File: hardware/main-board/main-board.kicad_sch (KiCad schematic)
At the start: 79 parts, among them J1 Conn_01x04_Socket, J2 Conn_01x04_Socket, J3 Conn_01x04_Socket, J4 Conn_01x04_Socket, J5 USB_C_Receptacle_USB2.0_16P, J6 Conn_01x02_MountingPin, J7 Conn_01x07_Socket, Q1 DMG2305UX, SW1 SW_SPDT, SW3 SW_SPDT, SW5 SW_Push, SW66 SW_Push, SW7 SW_Push, SW8 SW_Push, U1 ESP32-C6-MINI-1/U, U2 USBLC6-2SC6, U3 AP2112K-3.3, U4 TP4056-42-ESOP8, U5 AP22815AWT-7

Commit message: Added overvoltage protection to schematic
Layout Needs to be rerouted
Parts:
- renumbered D14 to D12, D12 to D8, F2 to F1
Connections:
- net +5V: no longer U2.5 (VBUS)
- net VBUS_PROTECTION_IN: now also U2.5 (VBUS)
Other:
- note added: "USB-C VBUS Protection with 1.5A Fuse"
- note added: "USB-C with ESD protection on D+ and D-"
- note removed: "Rename new parts with old numbering to keep parts"
- note removed: "U2 ESD protection Should be after VBUS protection or befor ?"
- note removed: "USB-C VBUS Protection"
- note removed: "USB-C with ESD Protection and 1.5A Fuse"
- moved on the sheet: C13, C14, C16, C3, C6, C9, D5, D6, D7, D8, F1, H1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

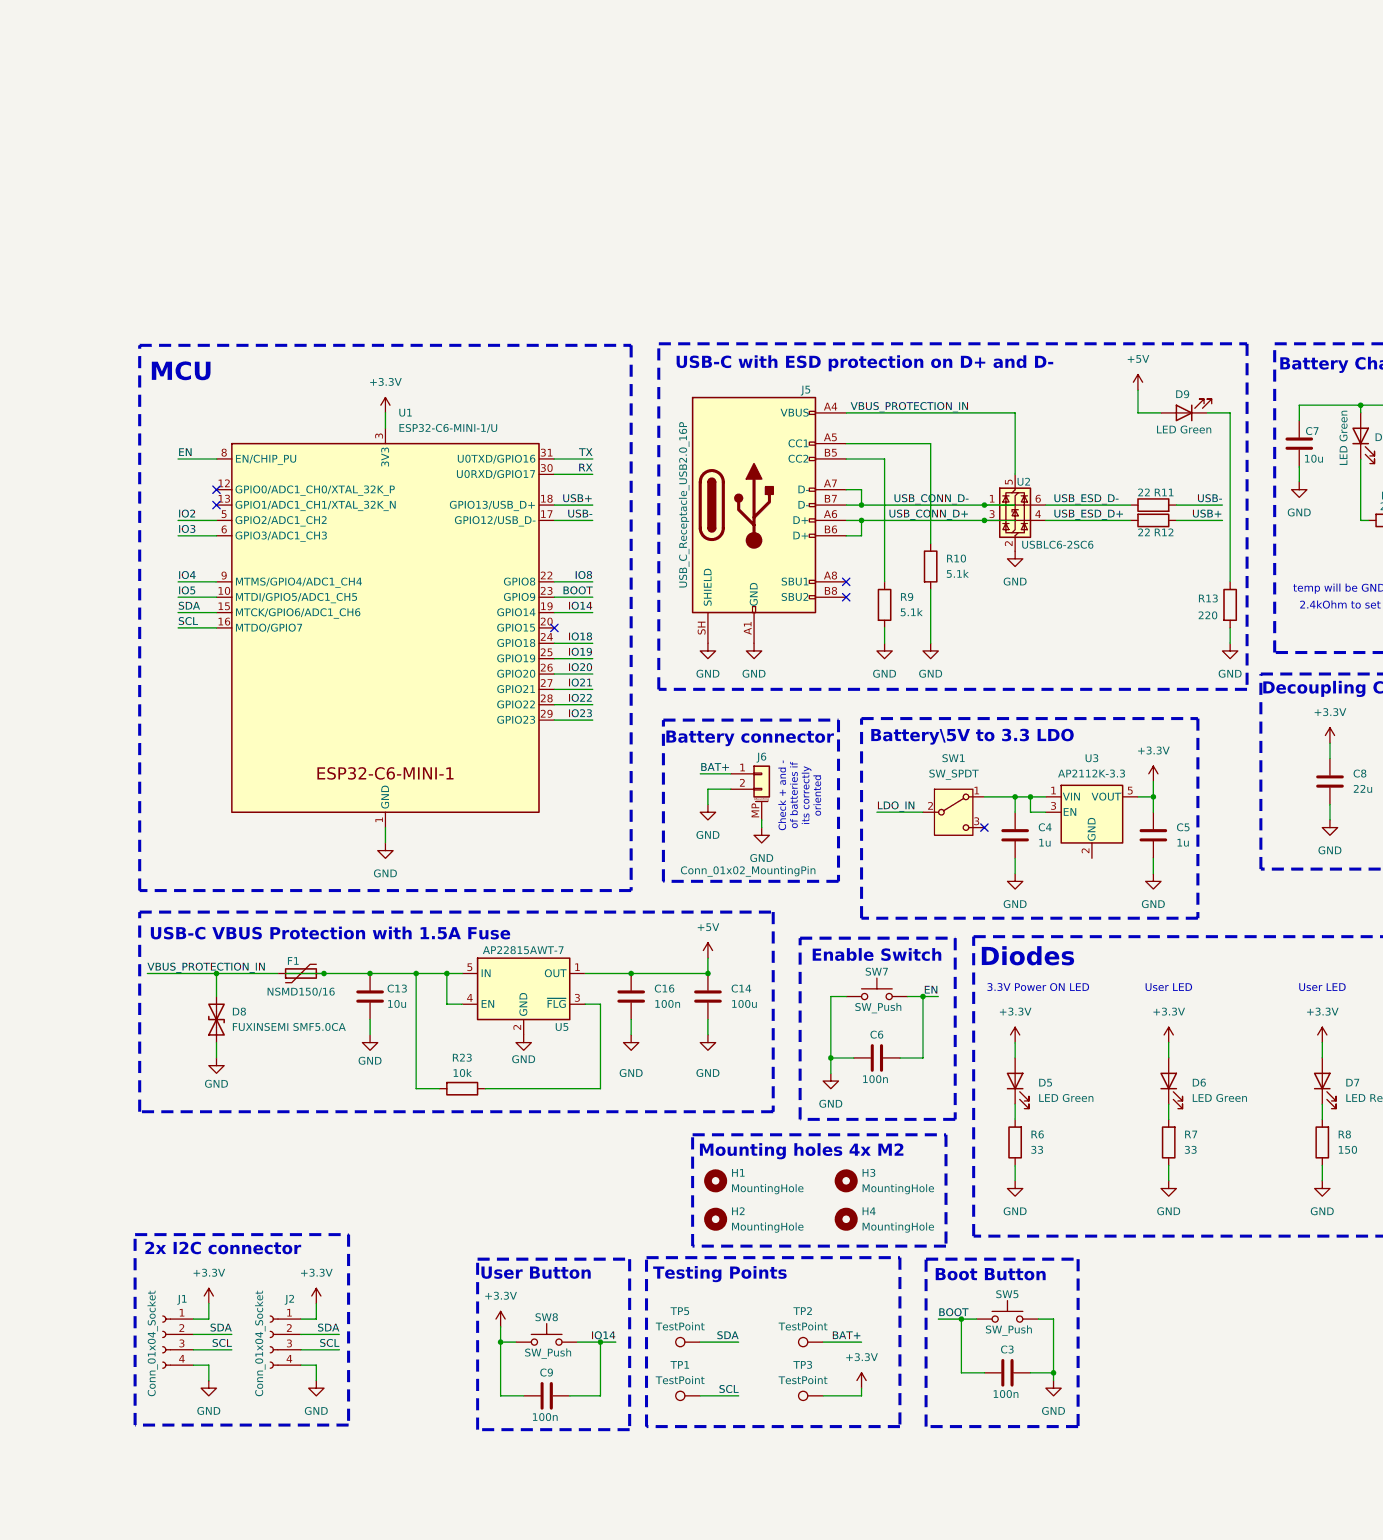
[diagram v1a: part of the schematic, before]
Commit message: After deciding we wont include OVP in this design, so i removed it from active schematic and check if everything is alright in pcb
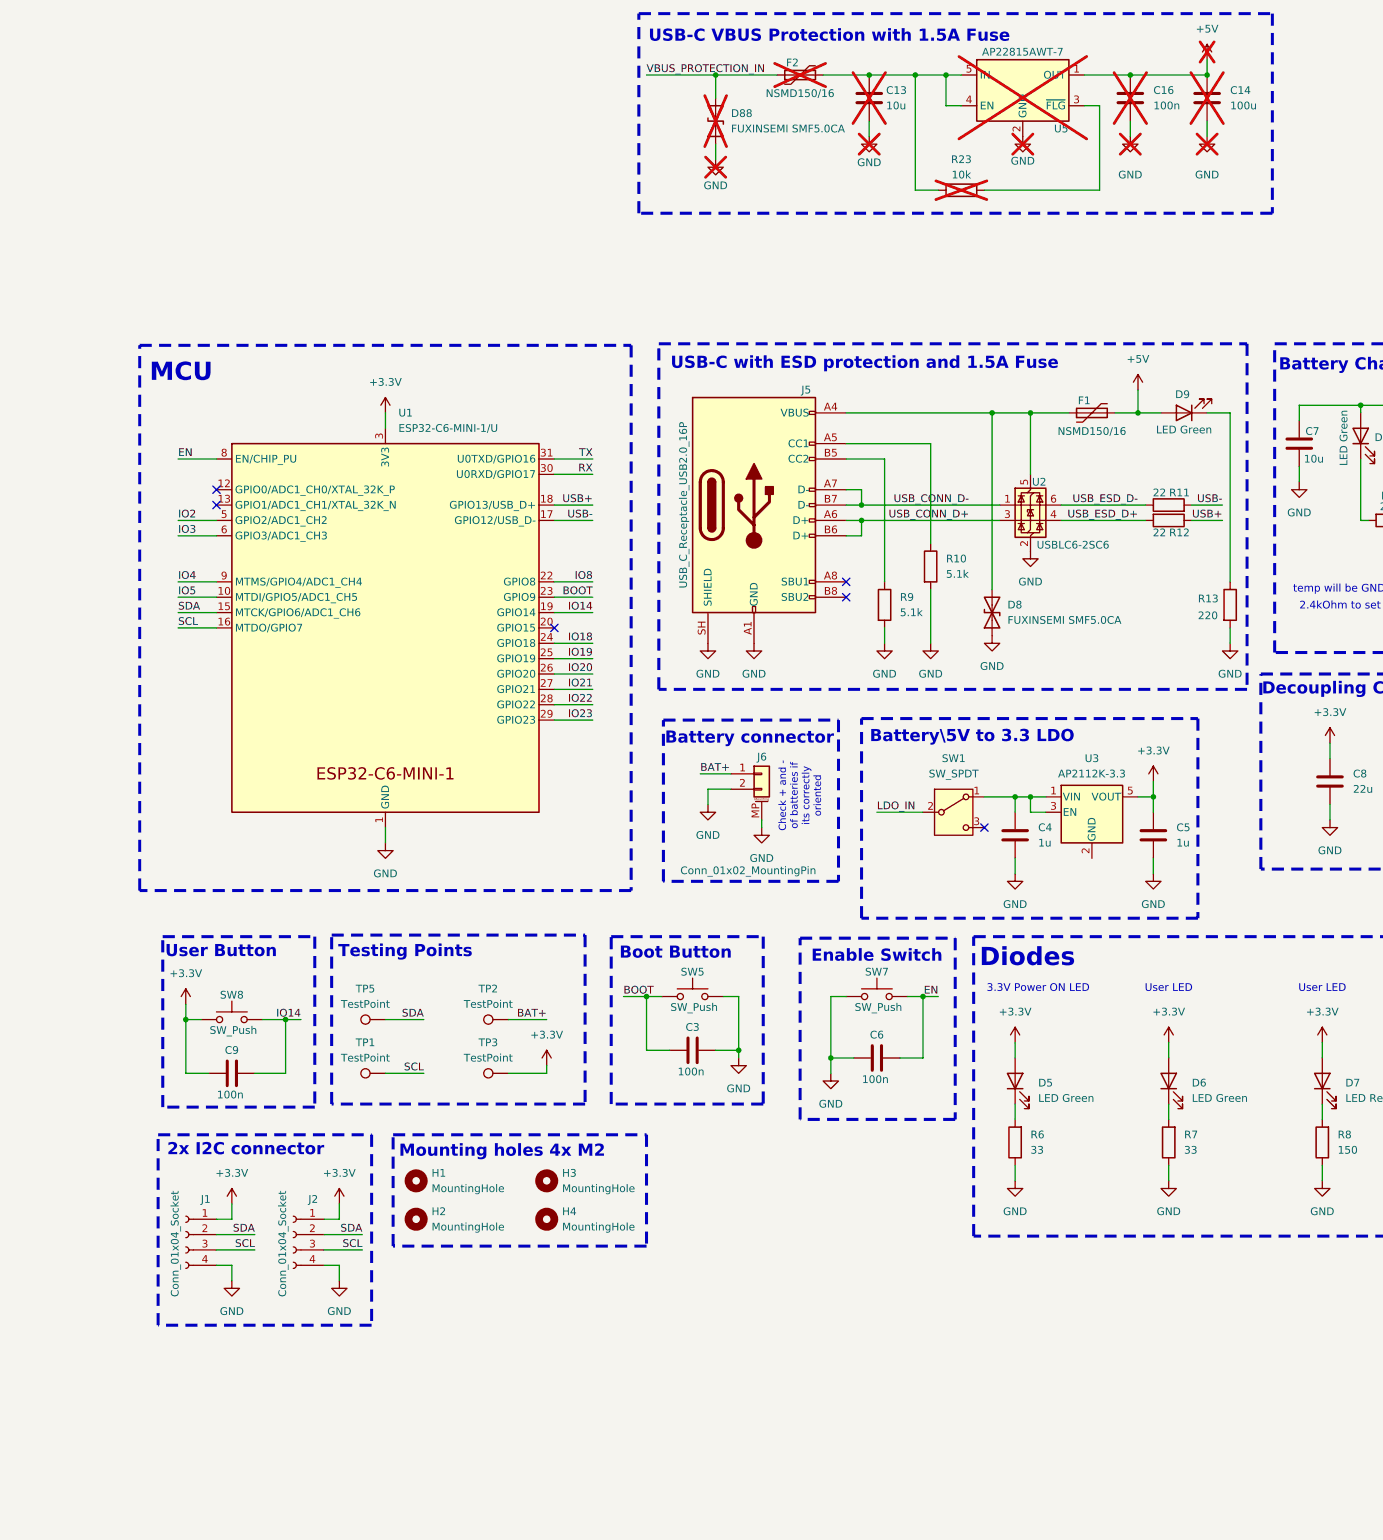
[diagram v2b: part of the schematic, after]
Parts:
- added D8: FUXINSEMI SMF5.0CA, Diode_SMD:D_SOD-123, symbol Device:D_TVS
- added F1: NSMD150/16, Fuse:Fuse_1206_3216Metric_Pad1.42x1.75mm_HandSolder, symbol Device:Polyfuse
- C13, C14, C16, R23, U5: now not fitted; now left out of the parts list
- D88: renamed from D8; now not fitted; now left out of the parts list
- F2: renamed from F1; now not fitted; now left out of the parts list
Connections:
- net +5V: now also F1.2
- net GND: now also D8.1 (A1)
- net VBUS_PROTECTION_IN: no longer J5.A4 (VBUS), J5.A9 (VBUS), J5.B4 (VBUS), J5.B9 (VBUS), U2.5 (VBUS)
- new net: D8.2 (A2), F1.1, J5.A4 (VBUS), J5.A9 (VBUS), J5.B4 (VBUS), J5.B9 (VBUS), U2.5 (VBUS)
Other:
- note added: "USB-C with ESD protection and 1.5A Fuse"
- note removed: "USB-C with ESD protection on D+ and D-"
- moved on the sheet: C3, C9, H1, H2, H3, H4, J1, J2, R11, R12, SW5, SW8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

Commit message: Added a python web for easier checking between BOM and supplier cart
I can make notes and check each part. It can be used on different
boards, the metadata is created/stored in each board project
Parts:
- SW5, SW7, SW8: value SW_Push -> XUNPU TS-1088-AR02016
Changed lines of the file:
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@@
 			)
 		)
-		(property "Value" "SW_Push"
+		(property "Value" "XUNPU TS-1088-AR02016"
 			(at 30.734 128.778 0)
 			(show_name no)
@@
 			)
 		)
-		(property "Datasheet" ""
+		(property "Datasheet" "https://www.lcsc.com/datasheet/C720477.pdf"
 			(at 30.48 121.92 0)
 			(hide yes)
@@
 			)
 		)
-		(property "Description" "Push button switch, generic, two pins"
+		(property "Description" "C720477 - SWITCH TACTILE SPST 160gf SMD"
 			(at 30.48 127 0)
 			(hide yes)
@@
 			)
 		)
-		(property "Value" "SW_Push"
+		(property "Value" "XUNPU TS-1088-AR02016"
 			(at 137.414 124.968 0)
 			(show_name no)
@@
 			)
 		)
-		(property "Datasheet" ""
+		(property "Datasheet" "https://www.lcsc.com/datasheet/C720477.pdf"
 			(at 137.16 118.11 0)
 			(hide yes)
@@
 			)
 		)
-		(property "Description" "Push button switch, generic, two pins"
+		(property "Description" "C720477 - SWITCH TACTILE SPST 160gf SMD"
 			(at 137.16 123.19 0)
 			(hide yes)
@@
 			)
 		)
-		(property "Value" "SW_Push"
+		(property "Value" "XUNPU TS-1088-AR02016"
 			(at 106.934 124.968 0)
 			(show_name no)
@@
 			)
 		)
-		(property "Datasheet" ""
+		(property "Datasheet" "https://www.lcsc.com/datasheet/C720477.pdf"
 			(at 106.68 118.11 0)
 			(hide yes)
@@
 			)
 		)
-		(property "Description" "Push button switch, generic, two pins"
+		(property "Description" "C720477 - SWITCH TACTILE SPST 160gf SMD"
 			(at 106.68 123.19 0)
 			(hide yes)
